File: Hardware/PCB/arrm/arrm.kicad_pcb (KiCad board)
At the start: 2 copper layers, 46 x 161 mm, 50 parts, among them J1 3_pin_Molex_header, J10 AudioJack2, J11 Synth_power_2x5, J3 2_pin_Molex_header, J5 2_pin_Molex_header, J7 AudioJack2, J8 AudioJack2, J9 AudioJack2, U1 NE5532, U2 TL072

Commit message: Rename project, cleanup
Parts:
- R12: value 33k -> 10k
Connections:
- net /Main PCB/CARRLVL_CW renamed /Main PCB/CARRLVL_WIP
- net /Main PCB/SIGLVL_CW renamed /Main PCB/SIGLVL_WIP
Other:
- board text added: "AC CAR IN"
- board text added: "Active Real Ring Modulator by Ken Stone PCB by Rich Holmes Mar 2022 https://github.com/holmesrichards/arrm"
- board text added: "CAR WIP"
- board text added: "CCW"
- board text added: "CW"
- board text added: "DC CAR IN"
- board text added: "OUT"
- board text added: "SIG CCW"
- board text added: "SIG IN"
- board text added: "UNB CCW"
- board text added: "WIP"

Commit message: Final pre fab tweaks, Gerbers
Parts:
- moved GRAF1 2.54 mm to (100.0, 100.0)
- renumbered C3 to C1, C5 to C10, C2 to C11, C4 to C2, C6 to C3, C9 to C4, C7 to C5, C10 to C6, C1 to C7, C11 to C9, D5 to D1, D6 to D2, D2 to D3, D1 to D4, D4 to D5, D3 to D6, J9 to J10, J10 to J11, J3 to J2, J5 to J3, J11 to J7, J7 to J8, J8 to J9, R8 to R1, R6 to R10, R12 to R11, R5 to R12, R4 to R2, R7 to R3, R9 to R4, R10 to R5, R1 to R6, R2 to R7, R11 to R8, R3 to R9, RV7 to RV4, RV8 to RV5, RV9 to RV6

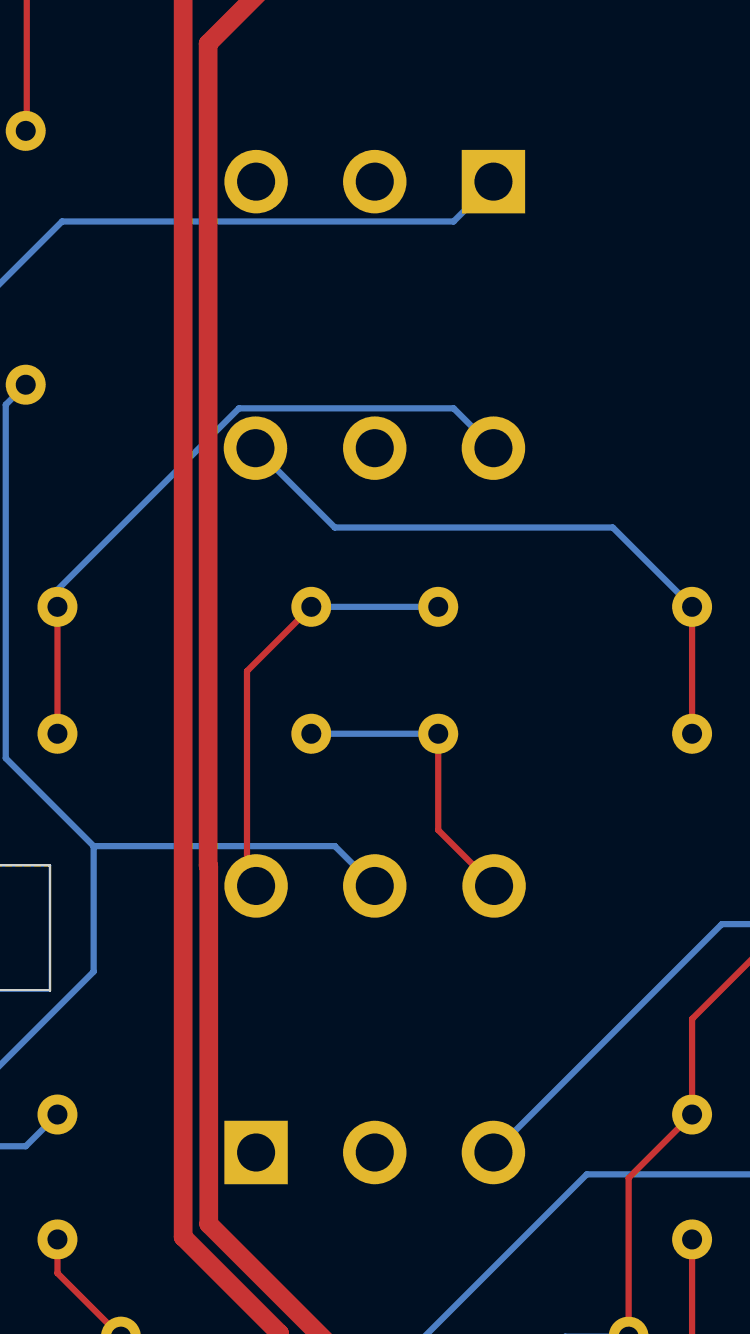
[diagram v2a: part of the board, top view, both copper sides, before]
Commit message: Fix footprint path; fix transformer footprint
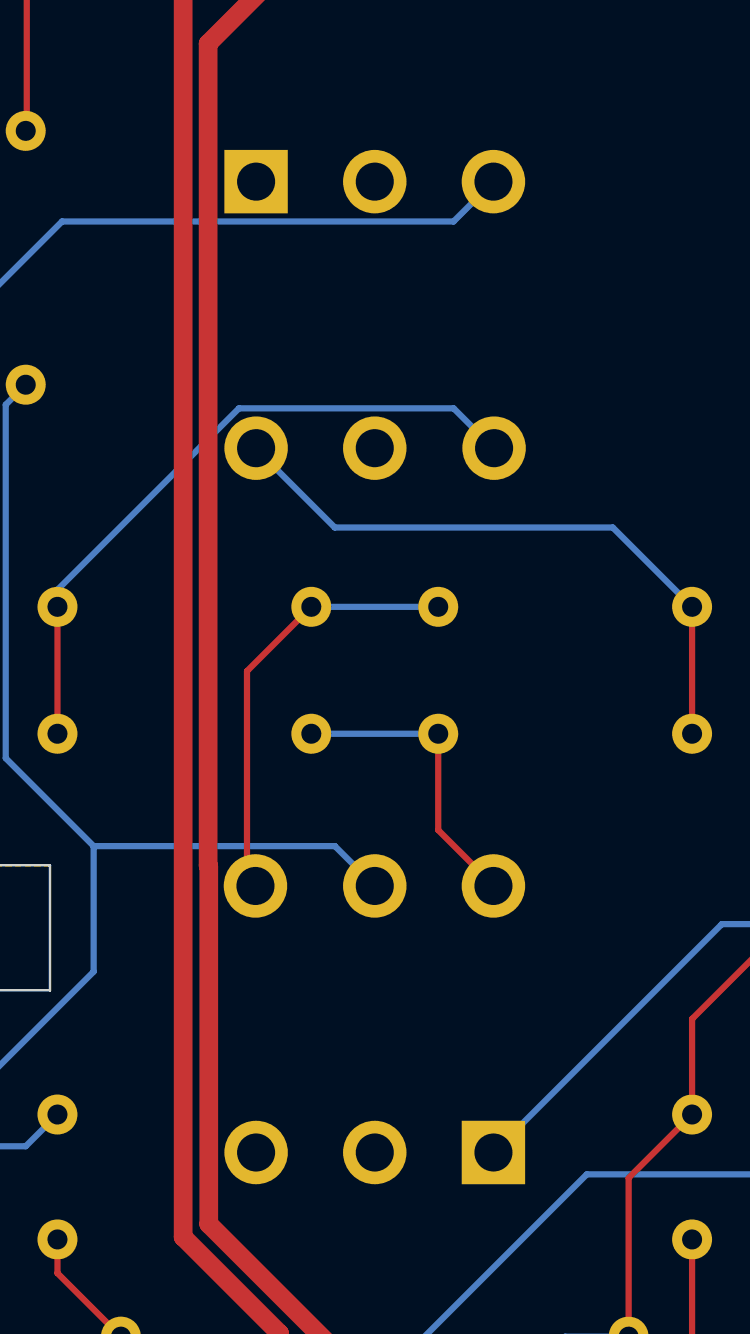
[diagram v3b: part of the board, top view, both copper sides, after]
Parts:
- moved TR1 9.50 mm to (104.7, 115.5), turned to 90 degrees
- moved TR2 9.50 mm to (95.3, 76.6), turned to -90 degrees
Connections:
- TR1 pad 1: GND -> /Main PCB/SIGLVL_WIP
- TR1 pad 3: /Main PCB/SIGLVL_WIP -> GND
- TR1 pad 4: Net-(D4-Pad2) -> Net-(D3-Pad1)
- TR1 pad 6: Net-(D3-Pad1) -> Net-(D4-Pad2)
- TR2 pad 1: Net-(R10-Pad1) -> GND
- TR2 pad 3: GND -> Net-(R10-Pad1)
- TR2 pad 4: Net-(D5-Pad1) -> Net-(D3-Pad2)
- TR2 pad 6: Net-(D3-Pad2) -> Net-(D5-Pad1)

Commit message: R4 should be 330k
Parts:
- R4: value 330R -> 330k
